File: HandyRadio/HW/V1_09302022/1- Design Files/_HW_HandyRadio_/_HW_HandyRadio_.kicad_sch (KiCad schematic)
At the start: 0 parts

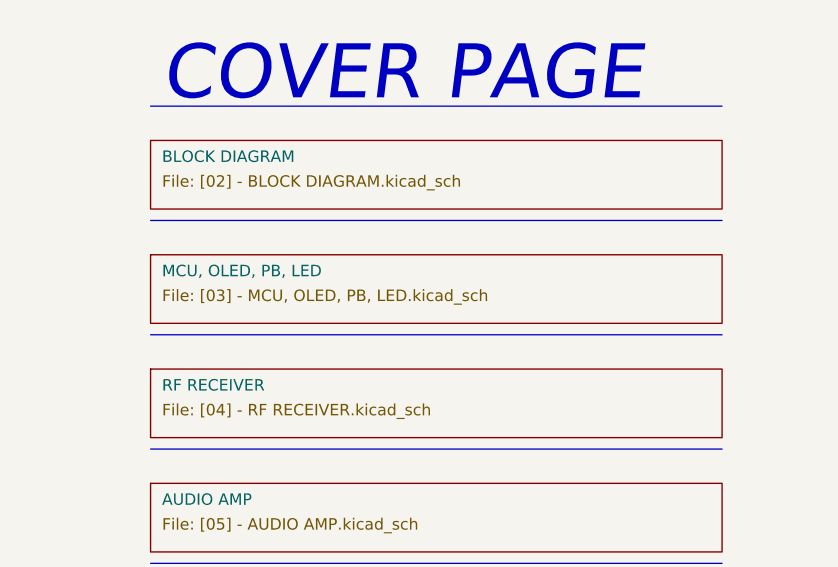
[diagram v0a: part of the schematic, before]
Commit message: HandyRadio BlockDiagram has been done
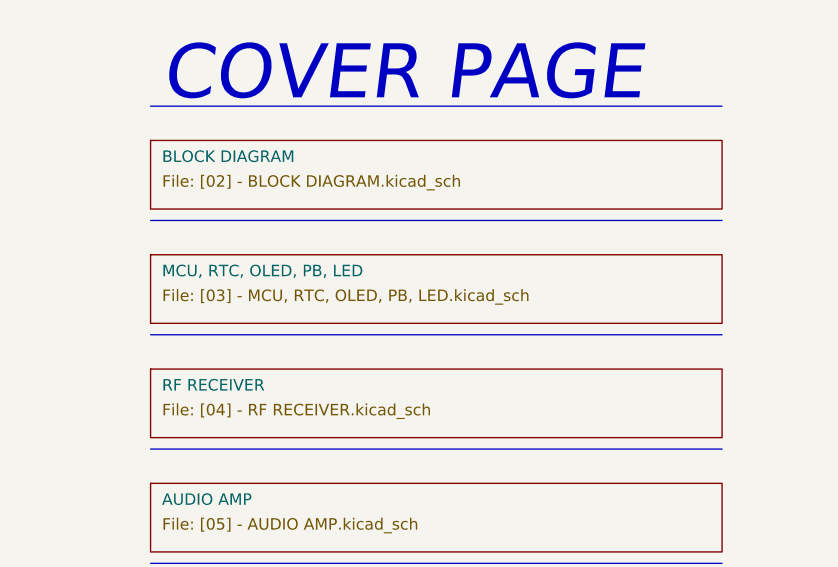
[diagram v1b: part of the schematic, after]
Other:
- sheet MCU, OLED, PB, LED renamed MCU, RTC, OLED, PB, LED
- sheet MCU, RTC, OLED, PB, LED: file [03] - MCU, OLED, PB, LED.kicad_sch -> [03] - MCU, RTC, OLED, PB, LED.kicad_sch
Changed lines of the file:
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@@
     (stroke (width 0.1524) (type solid) (color 0 0 0 0))
     (fill (color 0 0 0 0.0000))
-    (property "Sheet name" "MCU, OLED, PB, LED" (id 0) (at 63.5 158.75 0)
+    (property "Sheet name" "MCU, RTC, OLED, PB, LED" (id 0) (at 63.5 158.75 0)
       (effects (font (size 1.27 1.27)) (justify left bottom))
     )
-    (property "Sheet file" "[03] - MCU, OLED, PB, LED.kicad_sch" (id 1) (at 63.5 160.02 0)
+    (property "Sheet file" "[03] - MCU, RTC, OLED, PB, LED.kicad_sch" (id 1) (at 63.5 160.02 0)
       (effects (font (size 1.27 1.27)) (justify left top))
     )

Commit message: Schematic is almost Done
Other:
- added sheet REVISION HISTORY ([08] - REVISION HISTORY.kicad_sch)
- note removed: "PWR SEQUENCE"
- note removed: "REVISION HISTORY"
